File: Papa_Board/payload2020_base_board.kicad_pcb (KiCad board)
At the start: 4 copper layers, 82 x 82 mm, 101 parts, among them J1 1862, J10 1862, J11 Conn_01x05, J2 Conn_01x05, J3 Conn_01x05_Female, J4 Conn_01x05, J5 M80-5000642, J6 M80-5000642, J7 1862, J8 693072010801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

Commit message: Generate gerber files
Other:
- rule pad_to_mask_clearance: 0.0508 -> 0.051
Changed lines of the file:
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@@
   (page A4)
   (layers
-    (0 F.Cu signal)
+    (0 F.Cu signal hide)
     (1 GND.Cu power hide)
     (2 VCC.Cu power hide)
-    (31 B.Cu signal hide)
+    (31 B.Cu signal)
     (32 B.Adhes user hide)
     (33 F.Adhes user hide)
-    (34 B.Paste user hide)
-    (35 F.Paste user)
-    (36 B.SilkS user hide)
-    (37 F.SilkS user)
-    (38 B.Mask user hide)
-    (39 F.Mask user)
+    (34 B.Paste user)
+    (35 F.Paste user hide)
+    (36 B.SilkS user)
+    (37 F.SilkS user hide)
+    (38 B.Mask user)
+    (39 F.Mask user hide)
     (40 Dwgs.User user hide)
     (41 Cmts.User user hide)
@@
     (44 Edge.Cuts user)
     (45 Margin user hide)
-    (46 B.CrtYd user hide)
+    (46 B.CrtYd user)
     (47 F.CrtYd user hide)
-    (48 B.Fab user hide)
-    (49 F.Fab user)
+    (48 B.Fab user)
+    (49 F.Fab user hide)
   )
   (setup
@@
     (pad_size 7 7)
     (pad_drill 3.5)
-    (pad_to_mask_clearance 0.0508)
+    (pad_to_mask_clearance 0.051)
+    (solder_mask_min_width 0.25)
     (aux_axis_origin 0 0)
     (visible_elements 7FFFF7FF)
@@
       (drillshape 0)
       (scaleselection 1)
-      (outputdirectory "./"))
+      (outputdirectory "gerbers/"))
   )
   (net 0 "")
@@
       (effects (font (size 1 1) (thickness 0.15)))
     )
-    (fp_text user %R (at 0 0 90) (layer F.Fab)
-      (effects (font (size 0.8 0.8) (thickness 0.12)))
-    )
     (fp_line (start -1.6 0.8) (end -1.6 -0.8) (layer F.Fab) (width 0.1))
     (fp_line (start -1.6 -0.8) (end 1.6 -0.8) (layer F.Fab) (width 0.1))
@@
     (fp_line (start 2.48 -1.15) (end 2.48 1.15) (layer F.CrtYd) (width 0.05))
     (fp_line (start 2.48 1.15) (end -2.48 1.15) (layer F.CrtYd) (width 0.05))
-    (pad 2 smd roundrect (at 1.5625 0 270) (size 1.325 1.8) (layers F.Cu F.Paste F.Mask) (roundrect_rratio 0.188679)
+    (fp_text user %R (at 0 0 90) (layer F.Fab)
+      (effects (font (size 0.8 0.8) (thickness 0.12)))
+    )
+    (pad 2 smd roundrect (at 1.5625 0 270) (size 1.325 1.8) (layers F.Cu F.Paste F.Mask) (roundrect_rratio 0.1886777358490566)
       (net 1 GND))
-    (pad 1 smd roundrect (at -1.5625 0 270) (size 1.325 1.8) (layers F.Cu F.Paste F.Mask) (roundrect_rratio 0.188679)
+    (pad 1 smd roundrect (at -1.5625 0 270) (size 1.325 1.8) (layers F.Cu F.Paste F.Mask) (roundrect_rratio 0.1886777358490566)
       (net 5 +BATT))
     (model ${KISYS3DMOD}/Capacitor_SMD.3dshapes/C_1206_3216Metric.wrl
@@
       (effects (font (size 1 1) (thickness 0.15)))
     )
-    (fp_text user %R (at 0 0) (layer F.Fab)
-      (effects (font (size 0.8 0.8) (thickness 0.12)))
-    )
     (fp_line (start -1.6 0.8) (end -1.6 -0.8) (layer F.Fab) (width 0.1))
     (fp_line (start -1.6 -0.8) (end 1.6 -0.8) (layer F.Fab) (width 0.1))
@@
     (fp_line (start 2.48 -1.15) (end 2.48 1.15) (layer F.CrtYd) (width 0.05))
     (fp_line (start 2.48 1.15) (end -2.48 1.15) (layer F.CrtYd) (width 0.05))
-    (pad 2 smd roundrect (at 1.5625 0 180) (size 1.325 1.8) (layers F.Cu F.Paste F.Mask) (roundrect_rratio 0.188679)
+    (fp_text user %R (at 0 0) (layer F.Fab)
+      (effects (font (size 0.8 0.8) (thickness 0.12)))
+    )
+    (pad 2 smd roundrect (at 1.5625 0 180) (size 1.325 1.8) (layers F.Cu F.Paste F.Mask) (roundrect_rratio 0.1886777358490566)
       (net 1 GND))
-    (pad 1 smd roundrect (at -1.5625 0 180) (size 1.325 1.8) (layers F.Cu F.Paste F.Mask) (roundrect_rratio 0.188679)
+    (pad 1 smd roundrect (at -1.5625 0 180) (size 1.325 1.8) (layers F.Cu F.Paste F.Mask) (roundrect_rratio 0.1886777358490566)
       (net 76 /+37V))
     (model ${KISYS3DMOD}/Capacitor_SMD.3dshapes/C_1206_3216Metric.wrl
@@
       (effects (font (size 1 1) (thickness 0.15)))
     )
-    (fp_text user %R (at 0 0) (layer F.Fab)
-      (effects (font (size 0.8 0.8) (thickness 0.12)))
-    )
     (fp_line (start -1.6 0.8) (end -1.6 -0.8) (layer F.Fab) (width 0.1))
     (fp_line (start -1.6 -0.8) (end 1.6 -0.8) (layer F.Fab) (width 0.1))
@@
     (fp_line (start 2.48 -1.15) (end 2.48 1.15) (layer F.CrtYd) (width 0.05))
     (fp_line (start 2.48 1.15) (end -2.48 1.15) (layer F.CrtYd) (width 0.05))
-    (pad 2 smd roundrect (at 1.5625 0 180) (size 1.325 1.8) (layers F.Cu F.Paste F.Mask) (roundrect_rratio 0.188679)
+    (fp_text user %R (at 0 0) (layer F.Fab)
+      (effects (font (size 0.8 0.8) (thickness 0.12)))
+    )
+    (pad 2 smd roundrect (at 1.5625 0 180) (size 1.325 1.8) (layers F.Cu F.Paste F.Mask) (roundrect_rratio 0.1886777358490566)
       (net 1 GND))
-    (pad 1 smd roundrect (at -1.5625 0 180) (size 1.325 1.8) (layers F.Cu F.Paste F.Mask) (roundrect_rratio 0.188679)
+    (pad 1 smd roundrect (at -1.5625 0 180) (size 1.325 1.8) (layers F.Cu F.Paste F.Mask) (roundrect_rratio 0.1886777358490566)
       (net 76 /+37V))
     (model ${KISYS3DMOD}/Capacitor_SMD.3dshapes/C_1206_3216Metric.wrl
@@
       (effects (font (size 0.8 0.8) (thickness 0.12)))
     )
-    (pad 2 smd roundrect (at 1.55 0) (size 1.3 1.75) (layers F.Cu F.Paste F.Mask) (roundrect_rratio 0.192308)
+    (pad 2 smd roundrect (at 1.55 0) (size 1.3 1.75) (layers F.Cu F.Paste F.Mask) (roundrect_rratio 0.1923069230769231)
       (net 26 "Net-(F5-Pad2)"))
-    (pad 1 smd roundrect (at -1.55 0) (size 1.3 1.75) (layers F.Cu F.Paste F.Mask) (roundrect_rratio 0.192308)
+    (pad 1 smd roundrect (at -1.55 0) (size 1.3 1.75) (layers F.Cu F.Paste F.Mask) (roundrect_rratio 0.1923069230769231)
       (net 11 +3V3))
     (model ${KISYS3DMOD}/Resistor_SMD.3dshapes/R_1206_3216Metric.wrl
@@
       (effects (font (size 0.8 0.8) (thickness 0.12)))
     )
-    (pad 2 smd roundrect (at 1.55 0) (size 1.3 1.75) (layers F.Cu F.Paste F.Mask) (roundrect_rratio 0.192308)
+    (pad 2 smd roundrect (at 1.55 0) (size 1.3 1.75) (layers F.Cu F.Paste F.Mask) (roundrect_rratio 0.1923069230769231)
       (net 25 "Net-(F4-Pad2)"))
-    (pad 1 smd roundrect (at -1.55 0) (size 1.3 1.75) (layers F.Cu F.Paste F.Mask) (roundrect_rratio 0.192308)
+    (pad 1 smd roundrect (at -1.55 0) (size 1.3 1.75) (layers F.Cu F.Paste F.Mask) (roundrect_rratio 0.1923069230769231)
       (net 5 +BATT))
     (model ${KISYS3DMOD}/Resistor_SMD.3dshapes/R_1206_3216Metric.wrl
@@
       (effects (font (size 0.5 0.5) (thickness 0.08)) (justify mirror))
     )
-    (pad 2 smd roundrect (at 1 0 180) (size 1.2 1.4) (layers B.Cu B.Paste B.Mask) (roundrect_rratio 0.208333)
+    (pad 2 smd roundrect (at 1 0 180) (size 1.2 1.4) (layers B.Cu B.Paste B.Mask) (roundrect_rratio 0.2083325)
       (net 85 "Net-(Q3-Pad2)"))
-    (pad 1 smd roundrect (at -1 0 180) (size 1.2 1.4) (layers B.Cu B.Paste B.Mask) (roundrect_rratio 0.208333)
+    (pad 1 smd roundrect (at -1 0 180) (size 1.2 1.4) (layers B.Cu B.Paste B.Mask) (roundrect_rratio 0.2083325)
       (net 34 /5.3V_OUT))
     (model ${KISYS3DMOD}/Resistor_SMD.3dshapes/R_0805_2012Metric.wrl
@@
       (effects (font (size 0.5 0.5) (thickness 0.08)) (justify mirror))
     )
-    (pad 2 smd roundrect (at 1 0 90) (size 1.2 1.4) (layers B.Cu B.Paste B.Mask) (roundrect_rratio 0.208333)
+    (pad 2 smd roundrect (at 1 0 90) (size 1.2 1.4) (layers B.Cu B.Paste B.Mask) (roundrect_rratio 0.2083325)
       (net 75 /+5.3V))
-    (pad 1 smd roundrect (at -1 0 90) (size 1.2 1.4) (layers B.Cu B.Paste B.Mask) (roundrect_rratio 0.208333)
+    (pad 1 smd roundrect (at -1 0 90) (size 1.2 1.4) (layers B.Cu B.Paste B.Mask) (roundrect_rratio 0.2083325)
       (net 10 /5V3_ALWAYS_ON))
     (model ${KISYS3DMOD}/Resistor_SMD.3dshapes/R_0805_2012Metric.wrl
@@
   (via (at 106.88574 92.3544) (size 0.8) (drill 0.4) (layers F.Cu B.Cu) (net 10))
   (via (at 114.5032 119.7864) (size 0.8) (drill 0.4) (layers F.Cu B.Cu) (net 10))
-  (via (at 98.27768 97.6376) (size 0.8) (drill 0.4) (layers F.Cu B.Cu) (net 10))
+  (via (at 98.3996 97.5868) (size 0.8) (drill 0.4) (layers F.Cu B.Cu) (net 10))
   (segment (start 97.5487 103.3913) (end 97.5487 102.700624) (width 0.5) (layer B.Cu) (net 10))
   (segment (start 97.4852 102.8833) (end 97.4852 101.4984) (width 0.42) (layer B.Cu) (net 10))
@@
     )
   )
-  (zone (net 1) (net_name GND) (layer B.Cu) (hatch edge 0.508)
-    (priority 1)
-    (connect_pads (clearance 0.508))
-    (min_thickness 0.254)
-    (fill yes (arc_segments 32) (thermal_gap 0.508) (thermal_bridge_width 0.508) (smoothing chamfer) (radius 1))
-    (polygon
-      (pts
-        (xy 96.27616 84.80806) (xy 91.567 84.7852) (xy 91.567 85.9282) (xy 95.3516 86.0044) (xy 97.0661 87.9983)
-        (xy 97.0407 90.0557) (xy 95.0468 91.7702) (xy 94.21622 91.79814) (xy 94.234 94.8182) (xy 88.392 94.78645)
-        (xy 88.392 91.64955) (xy 86.4616 91.6051) (xy 84.997926 90.090625) (xy 85.0138 87.6046) (xy 86.3854 85.979)
-        (xy 87.757 86.0044) (xy 87.757 84.6582) (xy 84.72678 84.70646) (xy 83.98256 87.15756) (xy 84.0105 93.4974)
-        (xy 86.106 95.8342) (xy 96.977835 95.782765) (xy 98.541205 92.736035) (xy 98.47072 87.22868)
-      )
-    )
-  )
   (zone (net 10) (net_name /5V3_ALWAYS_ON) (layer VCC.Cu) (hatch edge 0.508)
     (connect_pads yes (clearance 0.2))
@@
       )
     )
-  )
-  (zone (net 1) (net_name GND) (layer B.Cu) (hatch edge 0.508)
-    (priority 2)
-    (connect_pads (clearance 0.2))
-    (min_thickness 0.254)
-    (fill yes (arc_segments 32) (thermal_gap 0.508) (thermal_bridge_width 0.508) (smoothing chamfer) (radius 1))
-    (polygon
-      (pts
-        (xy 95.8088 118.1862) (xy 94.5388 118.1862) (xy 92.7608 119.8626) (xy 92.7608 121.8438) (xy 94.361 123.7996)
-        (xy 95.25 123.825) (xy 95.3008 126.6444) (xy 102.489 126.619) (xy 102.4636 123.7742) (xy 103.5304 123.7234)
-        (xy 104.902 121.5898) (xy 104.9147 119.9134) (xy 103.0732 118.1862) (xy 101.727 118.237) (xy 101.727 117.6782)
-        (xy 106.1466 117.7036) (xy 106.1212 127.508) (xy 91.7448 127.508) (xy 91.7448 117.1702) (xy 95.8088 117.1702)
-      )
-    )

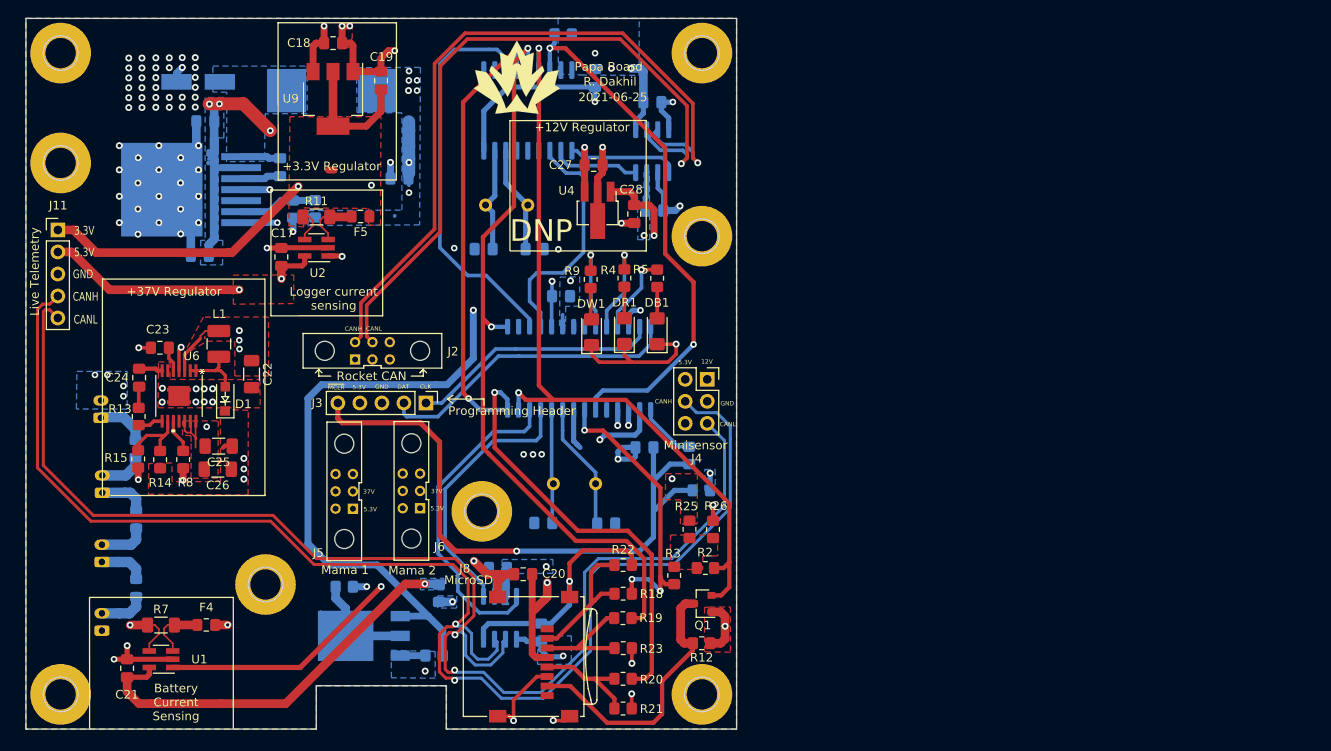
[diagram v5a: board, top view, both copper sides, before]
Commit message: Address Zach's review, just need to add more dimensions
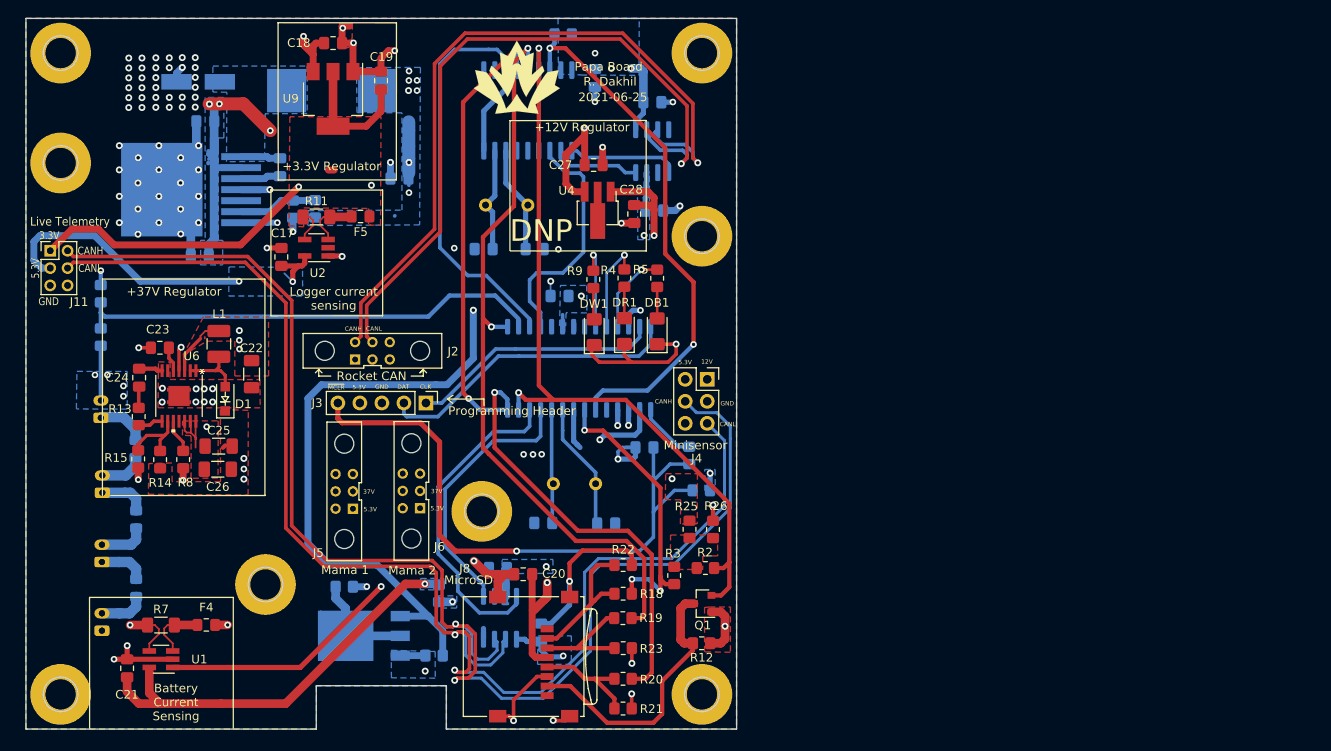
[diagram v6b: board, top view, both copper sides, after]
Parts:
- added R29: 30k, Resistor_SMD:R_0805_2012Metric_Pad1.20x1.40mm_HandSolder, B.Cu at (44.2, 104.1)
- added R30: 10k, Resistor_SMD:R_0805_2012Metric_Pad1.20x1.40mm_HandSolder, B.Cu at (44.2, 99.1)
- J11: footprint Connector_PinHeader_2.54mm:PinHeader_1x05_P2.54mm_Vertical -> Payload2020_custom:PinHeader_2x03_P2.00mm_Vertical_Harwin_Spacing
- moved J11 2.56 mm to (38.4, 94.1)
- moved DW1 0.30 mm to (101.1, 103.5)
- moved R9 0.30 mm to (101.0, 97.4)
- moved C11 0.18 mm to (97.1, 99.3)
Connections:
- U8 pad 16: Net-(U8-Pad16) -> V_SENSE
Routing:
- net V_SENSE: track 0.00 -> 54.4 mm
- net GND: track 195.5 -> 156.3 mm, vias 94 -> 95
- net +BATT: track 100.1 -> 113.7 mm
- net /+5.3V: track 89.1 -> 100.5 mm
- net +12V: track 29.2 -> 31.9 mm
- net +3V3: track 173.6 -> 174.8 mm
- net /CANH_PAYLOAD: track 163.6 -> 164.3 mm
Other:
- board text added: "+"
- board text added: "-"
- board text added: "31.75 mm"

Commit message: Add more dimensions
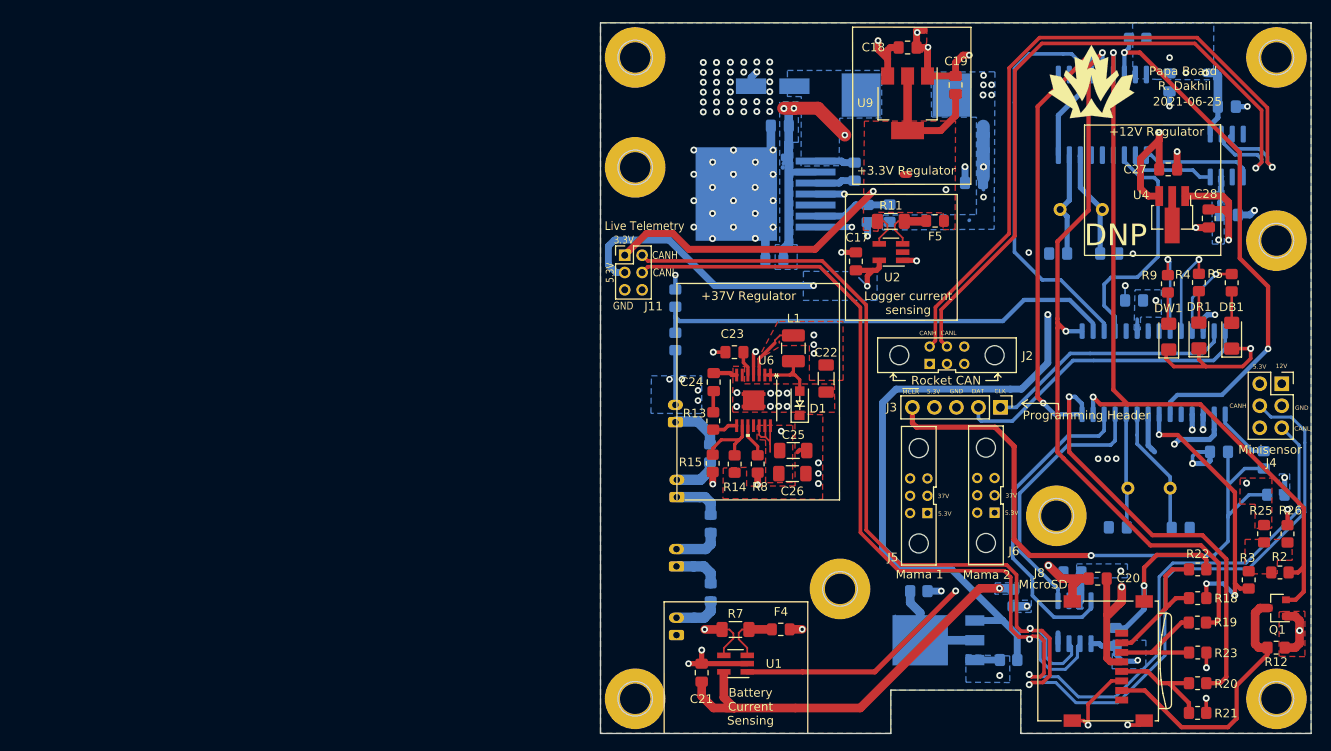
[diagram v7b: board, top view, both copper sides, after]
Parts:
- moved C14 66.3 mm to (161.3, 138.7)
- moved C15 66.3 mm to (174.3, 90.0)
- moved C25 66.3 mm to (124.1, 117.2)
- moved C5 66.3 mm to (122.6, 79.7)
- moved C6 66.3 mm to (131.2, 85.0)
- moved C7 66.3 mm to (145.0, 86.3)
- moved DB1 66.3 mm to (174.7, 103.9)
- moved DW1 66.3 mm to (167.4, 104.0)
- moved F4 66.3 mm to (122.7, 137.8)
- moved J1 66.3 mm to (110.5, 113.9)
- moved J11 66.3 mm to (104.7, 94.6)
- moved J5 66.3 mm to (138.6, 122.4)
- moved J7 66.3 mm to (110.7, 122.5)
- moved J8 66.3 mm to (164.6, 148.3)
- moved L1 66.3 mm to (124.1, 105.4)
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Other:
- board text added: "The 4 corner holes are all 4 mm from the edges"
